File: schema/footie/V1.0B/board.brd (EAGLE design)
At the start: 78.4 x 81.3 mm, 38 parts, among them T1 2N3565, U2 USD-SOCKETNEW, U3 HC_05, U4 MCP73831, U5 3.3 regulator, U6 ATMEGA328P-AU

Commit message: fix version 1.0B
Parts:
- removed JP1: RA 6Pin SMD, SparkFun-Connectors:1X06-SMD
- added U$2: JST_VERTICAL, SparkFun-Connectors:JST-6-SMD-VERT-1.0MM
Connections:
- net +3V3: now also U$2.4; no longer JP1.4
- net ARDUINO_RX: now also U$2.6; no longer JP1.6
- net ARDUINO_TX: now also U$2.5; no longer JP1.5
- net DTR: now also U$2.2; no longer JP1.2
- net GND: now also U$2.3; no longer JP1.3
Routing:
- net ARDUINO_RX: track 126.7 -> 150.2 mm, vias 6 -> 8
- net +3V3: track 288.8 -> 275.6 mm
- net GND: track 230.0 -> 219.2 mm, vias 30 -> 33
- net N$6: track 20.0 -> 14.6 mm
- net D10: track 12.2 -> 16.5 mm
- net ARDUINO_TX: track 96.5 -> 100.6 mm, vias 5 -> 8
- net GPSRX: track 51.9 -> 55.6 mm, vias 3 -> 2
- net DTR: track 89.7 -> 93.2 mm
- net N$20: track 43.2 -> 40.9 mm
- net GPSTX: track 48.4 -> 46.9 mm
- net SD_MISO: track 63.4 -> 64.4 mm
- net SD_MOSI: track 77.6 -> 78.3 mm
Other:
- board text added: "ARDUINO"
- board text added: "BATTERY"
- board text added: "BLUETOOTH"
- board text added: "BT"
- board text added: "GPS"
- board text added: "ISP"
- board text added: "PROGR"
- board text added: "RGB"
- board text added: "SDCARD"
- board text added: "START"
- board text added: "USB"

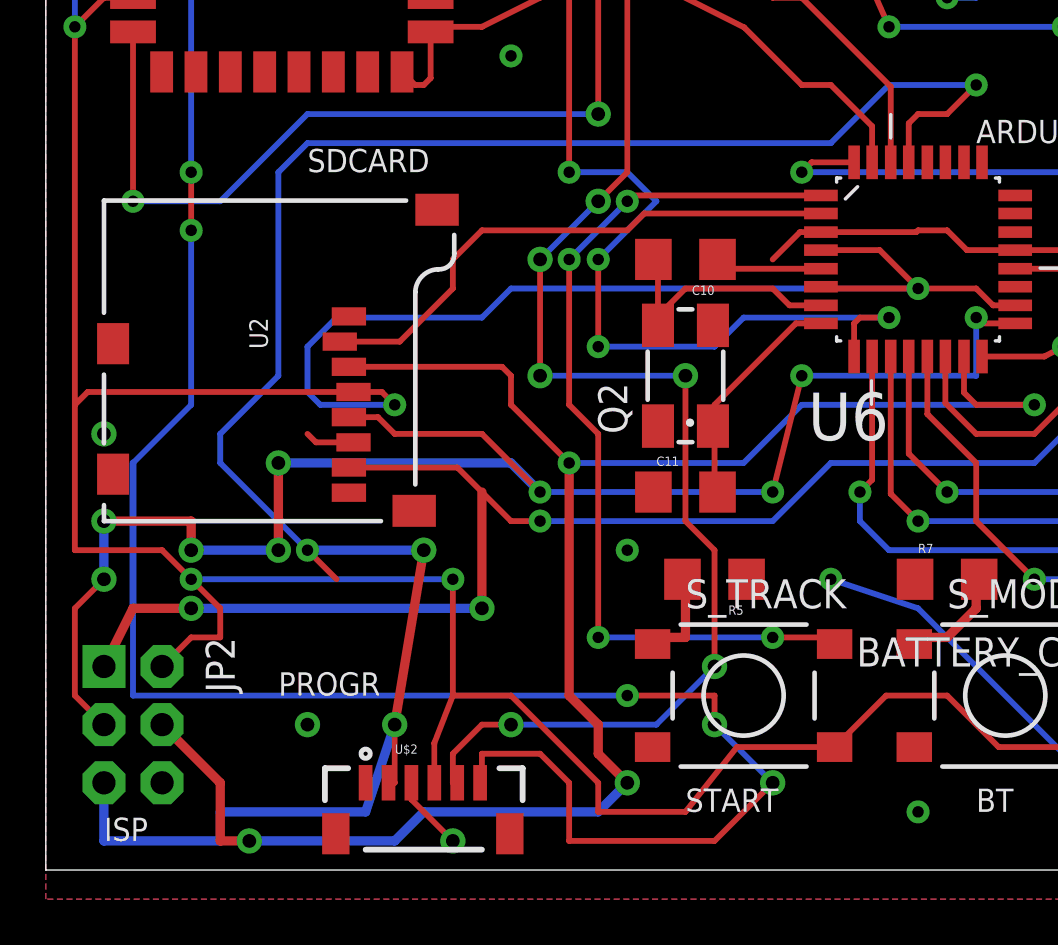
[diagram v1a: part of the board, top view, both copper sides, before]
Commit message: fix sdcard position add autoreset capacitor
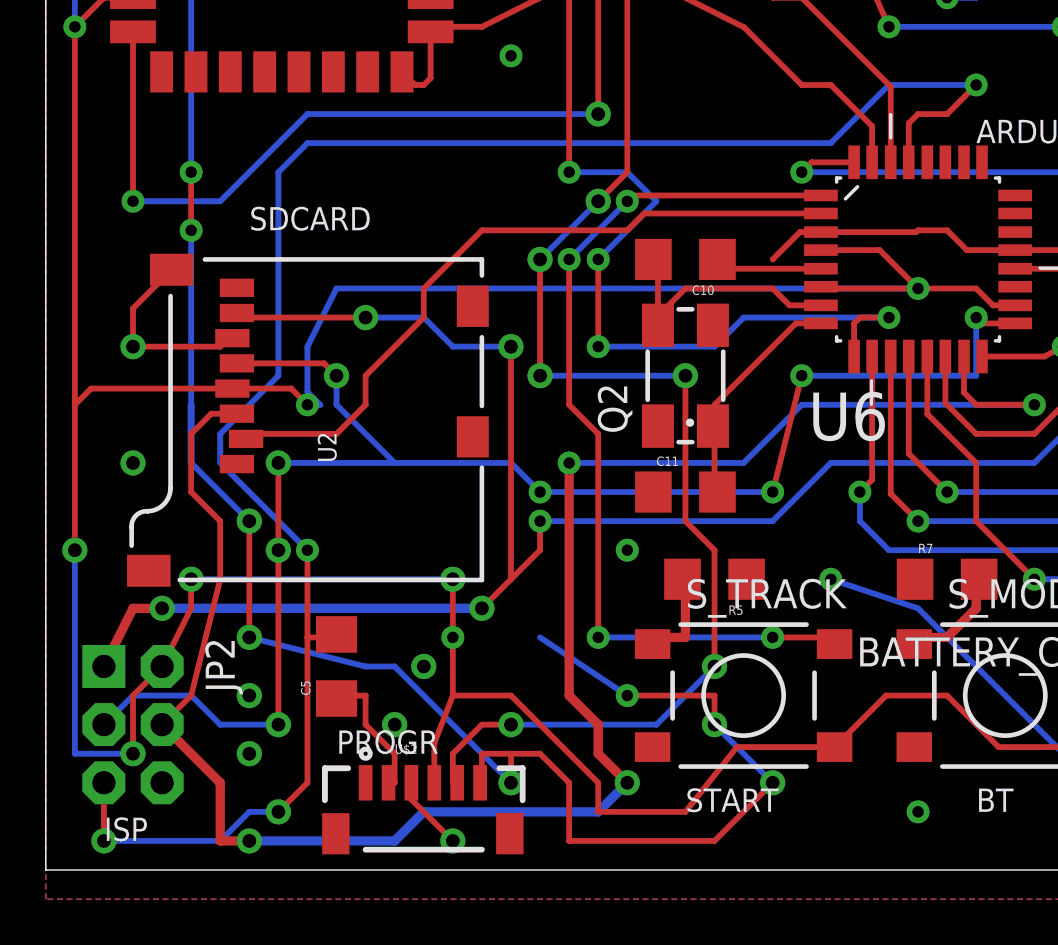
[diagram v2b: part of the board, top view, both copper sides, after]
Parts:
- added C5: 0.1 uF, SparkFun-Capacitors:1206
- moved U2 20.1 mm to (19.1, 26.7), turned to 90 degrees
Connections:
- new net N$13: C5.1, U$2.2
- net DTR: now also C5.2; no longer U$2.2
- net GND: now also U2.GND1, U2.GND3
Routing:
- net SD_MISO: track 64.4 -> 77.5 mm, vias 4 -> 6
- net DTR: track 93.2 -> 80.6 mm
- net SD_CS: track 24.1 -> 30.7 mm
- net GND: track 219.2 -> 225.6 mm, vias 33 -> 37
- net N$13: track 0.00 -> 6.01 mm
- net ARDUINO_RX: track 150.2 -> 145.6 mm, vias 8 -> 11
- net SD_MOSI: track 78.3 -> 82.5 mm
- net SD_SCK: track 71.7 -> 68.9 mm, vias 9 -> 8
- net +3V3: track 275.6 -> 277.9 mm, vias 9 -> 12

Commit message: add fix for reset add fix for sdcard add gerber files
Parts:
- added C6: 0.1 uF, SparkFun-Capacitors:1206
- added R10, R12, R14: 4.7k, SparkFun-Passives:1206
- added R11, R13, R15: 10k, SparkFun-Passives:1206
- added R4: 10K, SparkFun-Passives:1206
- moved MICRO_USB 1.27 mm to (71.1, 3.81)
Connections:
- new net N$14: R10.1, R11.2, U2.5
- new net N$17: R12.2, R13.1, U2.2
- new net N$26: R14.2, R15.1, U2.3
- net +3V3: now also C6.2, R4.1
- net DTR: now also R4.2
- net GND: now also C6.1, R11.1, R13.2, R15.2
- net SD_CS: now also R12.1; no longer U2.2
- net SD_MOSI: now also R14.1; no longer U2.3
- net SD_SCK: now also R10.2; no longer U2.5
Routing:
- net N$17: track 0.00 -> 76.7 mm, vias 0 -> 4
- net N$26: track 0.00 -> 64.1 mm, vias 0 -> 6
- net N$14: track 0.00 -> 50.0 mm, vias 0 -> 4
- net SD_MOSI: track 82.5 -> 131.2 mm, vias 4 -> 10
- net SD_CS: track 30.7 -> 52.9 mm, vias 0 -> 6
- net +3V3: track 277.9 -> 287.0 mm, vias 12 -> 13
- net GND: track 225.6 -> 233.7 mm, vias 37 -> 38
- net SD_SCK: track 68.9 -> 76.3 mm, vias 8 -> 7
- net DTR: track 80.6 -> 84.5 mm, vias 4 -> 5
- net D3: track 39.7 -> 43.6 mm
- net N$20: track 40.9 -> 38.4 mm
- net D5: track 51.0 -> 51.8 mm
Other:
- board text added: "FOOTIE 1.0B V"
- board text removed: "FOOTIE 1.0V"
